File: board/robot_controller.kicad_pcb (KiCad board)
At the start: 2 copper layers, 308 parts, among them J101 CONN_2, J102 CONN_2, J103 CONN_2, J104 JTAG-ARM, J105 CONN_2, J106 USBCONN, J107 CONN_8, J108 CONN_8, J109 USBCONN, J110 CONN_4, J111 UEXT, J112 UEXT, J201 CONN_2, J2301 CONN_STEPPER, J2302 CONN_2, J2401 CONN_STEPPER, J2402 CONN_2, J2501 CONN_STEPPER, J2502 CONN_2, J2601 CONN_STEPPER, J2602 CONN_2, J301 CONN_2, P101 CONN_4, P102 CONN_1, P103 CONN_1, P104 CONN_1, P105 CONN_1, P106 CONN_1, P107 CONN_1, P108 CONN_1, P109 CONN_1, P110 CONN_1, P111 CONN_1, P112 CONN_1, P113 CONN_1, P114 CONN_1, P115 CONN_1, P116 CONN_1, P117 CONN_1, P118 CONN_1, P119 CONN_1, P120 CONN_1, P121 CONN_1, P122 CONN_1, P123 CONN_1, P124 CONN_1, P125 CONN_1, P126 CONN_1, P127 CONN_1, P128 CONN_1, P129 CONN_1, P130 CONN_1, Q101 PNP, Q1501 NJT4031NT1G, Q1601 NJT4031NT1G, Q1701 NJT4031NT1G, Q1801 NJT4031NT1G, Q1901 NJT4031NT1G, Q2001 NJT4031NT1G, Q2101 NJT4031NT1G, Q2201 NJT4031NT1G, Q401 MMBT5962, Q402 MMBT5962, Q501 MMBT5962, Q502 MMBT5962, U101 STM32F405-144, U102 FT232RL, U201 MAX6675, U2301 L6470, U2401 L6470, U2501 L6470, U2601 L6470, U301 MAX6675, U601 LMZ14201, X101 8MHZ

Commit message: Layed out in general where stuff is going to be located.
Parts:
- moved J109 278.8 mm to (43.2, -112.4), turned to 270 degrees
- moved J2302 257.3 mm to (94.6, -38.1), turned to 180 degrees
- moved R2306 254.5 mm to (90.8, -45.1), turned to 270 degrees
- moved R2307 254.2 mm to (93.3, -45.1)
- moved C2304 248.3 mm to (77.8, -48.6)
- moved C2305 248.3 mm to (76.5, -76.2)
- moved C2306 248.3 mm to (76.5, -77.8)
- moved C2308 248.3 mm to (83.8, -77.8)
- moved C2309 248.3 mm to (69.8, -53.7)
- moved C2310 248.3 mm to (82.2, -53.7)
- moved C2311 248.3 mm to (92.4, -78.1)
- moved D2301 248.3 mm to (76.5, -47.9)
- moved R2301 248.3 mm to (71.8, -85.4)
- moved R2303 248.3 mm to (71.8, -81.6)
- moved R2305 248.3 mm to (68.3, -83.5)
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- renumbered P101 to J113
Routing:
- net GND: track 210.8 -> 261.8 mm, vias 77 -> 82
- net +24V: track 373.3 -> 344.6 mm, vias 49 -> 48
- net /LED Data 0/DATA_OUT: track 0.00 -> 16.4 mm
- net /LED Data 1/DATA_OUT: track 0.00 -> 10.3 mm
- net Net-(R127-Pad3): track 0.00 -> 8.26 mm
- net Net-(J2302-Pad2): track 0.00 -> 8.25 mm
- net Net-(Q501-Pad2): track 0.00 -> 7.61 mm
- net Net-(Q401-Pad2): track 0.00 -> 7.61 mm
- net /LED Data 1/DATA_IN: track 0.00 -> 7.13 mm
- net /Stepper 0/ADCIN: track 72.9 -> 79.8 mm
- net Net-(C2315-Pad1): track 36.1 -> 42.9 mm
- net /SUPPLY_SENSE: track 0.00 -> 5.47 mm
- net Net-(Q502-Pad2): track 0.00 -> 4.55 mm
- net +3.3V: track 199.3 -> 194.8 mm
- net Net-(Q402-Pad2): track 0.00 -> 4.28 mm
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
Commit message: Organized MCU components in the layout
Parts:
- moved R115 206.1 mm to (-59.1, 163.5)
- moved R116 170.6 mm to (39.4, 18.7)
- moved D103 140.6 mm to (152.4, 25.1)
- moved D102 137.1 mm to (152.4, 23.2)
- moved D105 122.6 mm to (155.3, 34.0)
- moved R107 117.2 mm to (155.9, 27.0)
- moved D101 115.4 mm to (152.4, 21.3)
- moved R104 113.2 mm to (155.9, 25.1)
- moved R106 112.7 mm to (152.4, 34.0), turned to 180 degrees
- moved R129 112.6 mm to (28.6, 47.9)
- moved X101 109.5 mm to (121.6, 109.2), turned to 270 degrees
- moved R113 103.8 mm to (33.0, 158.8)
- moved R114 101.3 mm to (124.1, 158.8)
- moved R102 100.5 mm to (155.9, 23.2)
- moved D104 96.6 mm to (152.4, 27.0)
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
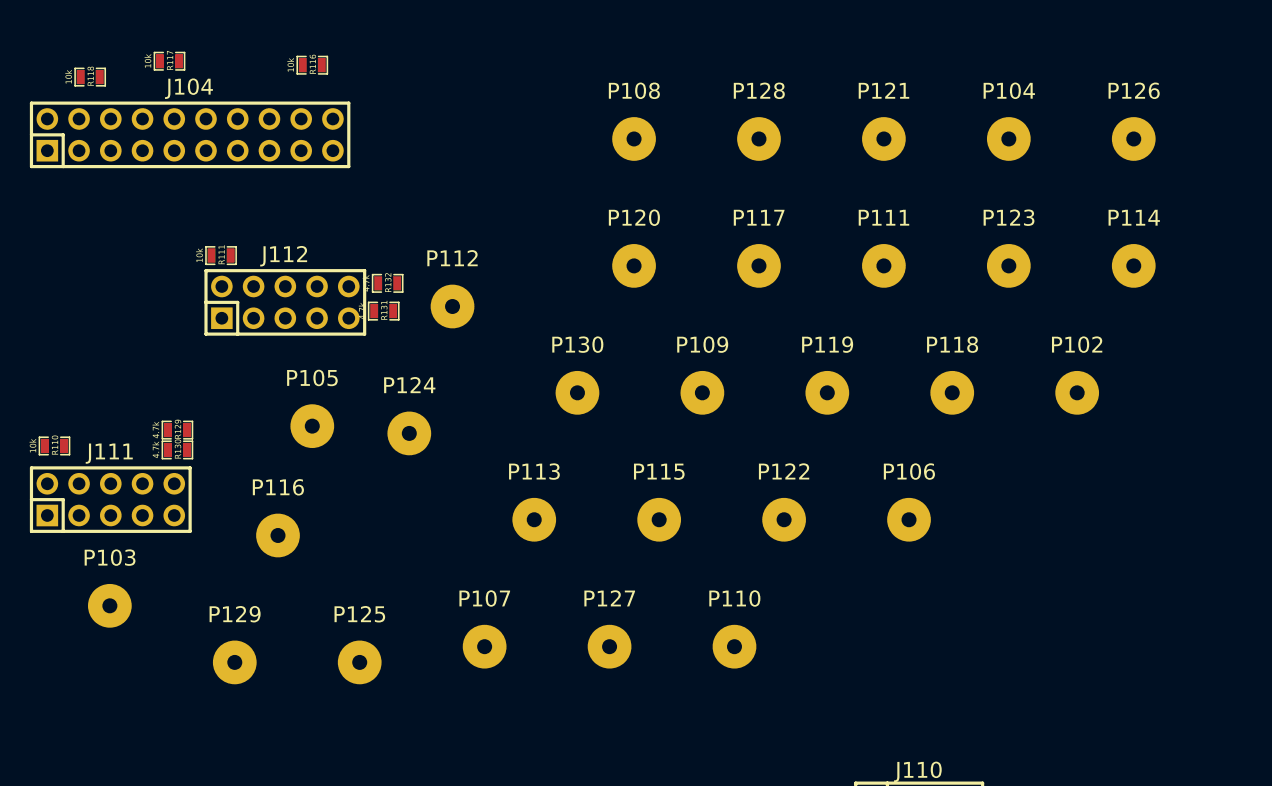
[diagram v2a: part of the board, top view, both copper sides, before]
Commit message: Updated Test Point Footprint on the PCB Layout
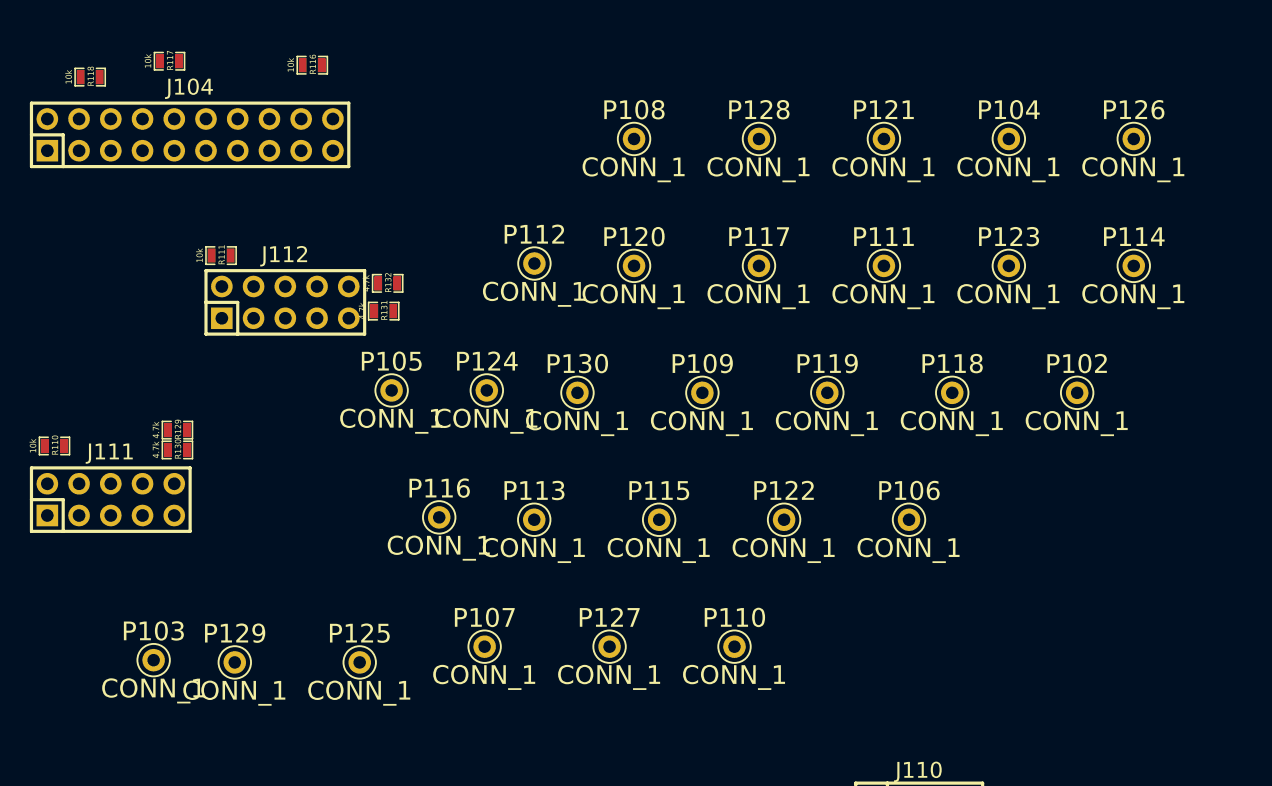
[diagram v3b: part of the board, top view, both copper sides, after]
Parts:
- P102, P103, P104, P105, P106, P107, P108, P109, P110, P111, P112, P113, P114, P115, P116, P117, P118, P119, P120, P121, P122, P123, P124, P125, P126, P127, P128, P129, P130: footprint Wire_Pads:SolderWirePad_single_1-2mmDrill -> components:MINI_TP
- moved P116 13.0 mm to (49.5, 54.9)
- moved P112 7.40 mm to (57.1, 34.6)
- moved P124 7.09 mm to (53.3, 44.8)
- moved P105 6.96 mm to (45.7, 44.8)
- moved P103 5.59 mm to (26.7, 66.4)

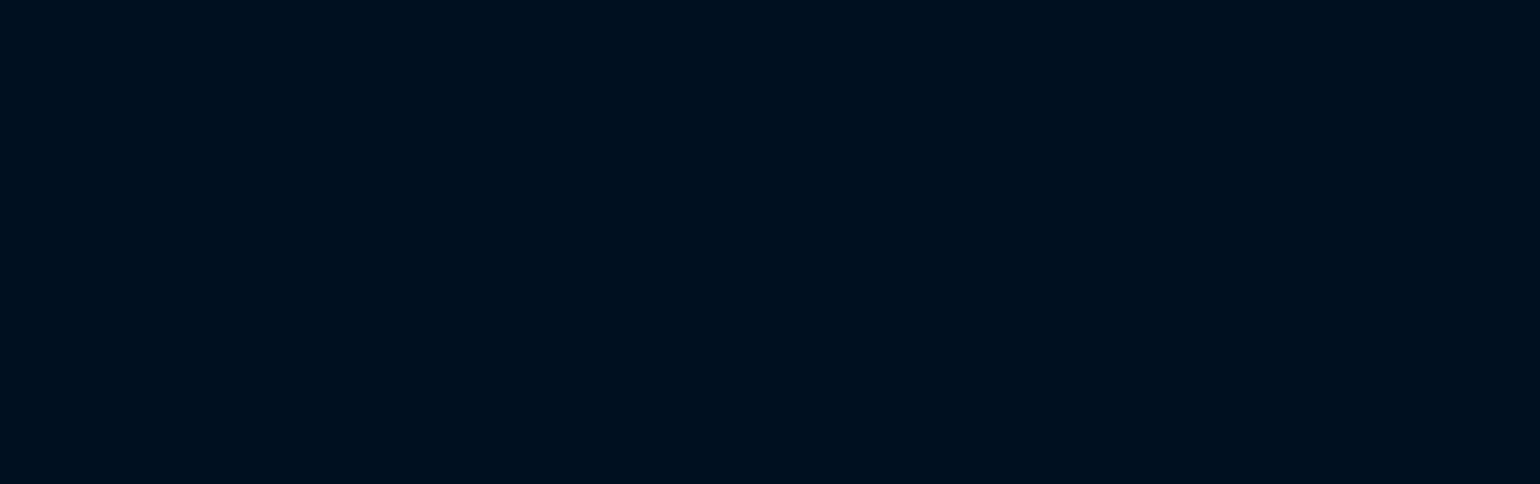
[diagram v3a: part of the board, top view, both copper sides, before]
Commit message: Added pushbuttons to the PCB Layout
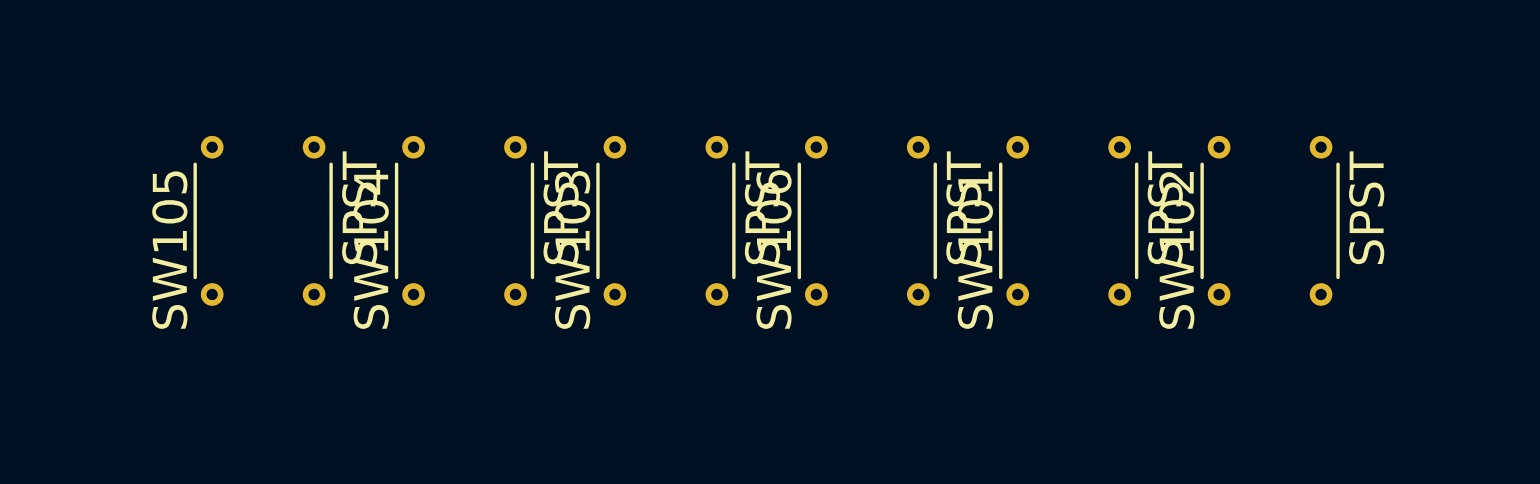
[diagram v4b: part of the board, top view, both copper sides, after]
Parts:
- added SW101: SPST, components:PB, F.Cu at (163.8, 61.3)
- added SW102: SPST, components:PB, F.Cu at (172.7, 61.3)
- added SW103: SPST, components:PB, F.Cu at (146.1, 61.3)
- added SW104: SPST, components:PB, F.Cu at (137.2, 61.3)
- added SW105: SPST, components:PB, F.Cu at (128.3, 61.3)
- added SW106: SPST, components:PB, F.Cu at (154.9, 61.3)
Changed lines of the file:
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@@
 (kicad_pcb (version 3) (host pcbnew "(2014-01-30 BZR 4648)-product")
   (general
-    (links 0)
-    (no_connects 582)
-    (area -73.4568 -152.779801 210.090657 201.0768)
+    (links 781)
+    (no_connects 606)
+    (area 0 0 0 0)
     (thickness 1.6)
     (drawings 0)
     (tracks 1030)
     (zones 0)
-    (modules 308)
+    (modules 314)
     (nets 238)
   )
@@
       (net 68 "/Stepper 0/SCK"))
   )
+  (module components:PB (layer F.Cu)
+    (at 163.83 61.2775)
+    (fp_text reference SW101 (at -4.064 1.27 90) (layer F.SilkS)
+      (effects (font (size 1.5 1.5) (thickness 0.15)))
+    )
+    (fp_text value SPST (at 4.318 -0.508 90) (layer F.SilkS)
+      (effects (font (size 1.5 1.5) (thickness 0.15)))
+    )
+    (fp_line (start 3 -2.5) (end 3 2.5) (layer F.SilkS) (width 0.15))
+    (fp_line (start -3 -2.5) (end -3 2.5) (layer F.SilkS) (width 0.15))
+    (pad 1 thru_hole circle (at -2.25 -3.25) (size 1 1) (drill 0.5) (layers *.Cu *.Mask F.SilkS)
+      (net 2 +3.3V))
+    (pad 1 thru_hole circle (at -2.25 3.25) (size 1 1) (drill 0.5) (layers *.Cu *.Mask F.SilkS)
+      (net 2 +3.3V))
+    (pad 2 thru_hole circle (at 2.25 3.25) (size 1 1) (drill 0.5) (layers *.Cu *.Mask F.SilkS)
+      (net 62 /SW0))
+    (pad 2 thru_hole circle (at 2.25 -3.25) (size 1 1) (drill 0.5) (layers *.Cu *.Mask F.SilkS)
+      (net 62 /SW0))
+  )
+  (module components:PB (layer F.Cu)
+    (at 172.72 61.2775)
+    (fp_text reference SW102 (at -4.064 1.27 90) (layer F.SilkS)
+      (effects (font (size 1.5 1.5) (thickness 0.15)))
+    )
+    (fp_text value SPST (at 4.318 -0.508 90) (layer F.SilkS)
+      (effects (font (size 1.5 1.5) (thickness 0.15)))
+    )
+    (fp_line (start 3 -2.5) (end 3 2.5) (layer F.SilkS) (width 0.15))
+    (fp_line (start -3 -2.5) (end -3 2.5) (layer F.SilkS) (width 0.15))
+    (pad 1 thru_hole circle (at -2.25 -3.25) (size 1 1) (drill 0.5) (layers *.Cu *.Mask F.SilkS)
+      (net 2 +3.3V))
+    (pad 1 thru_hole circle (at -2.25 3.25) (size 1 1) (drill 0.5) (layers *.Cu *.Mask F.SilkS)
+      (net 2 +3.3V))
+    (pad 2 thru_hole circle (at 2.25 3.25) (size 1 1) (drill 0.5) (layers *.Cu *.Mask F.SilkS)
+      (net 63 /SW1))
+    (pad 2 thru_hole circle (at 2.25 -3.25) (size 1 1) (drill 0.5) (layers *.Cu *.Mask F.SilkS)
+      (net 63 /SW1))
+  )
+  (module components:PB (layer F.Cu)
+    (at 146.05 61.2775)
+    (fp_text reference SW103 (at -4.064 1.27 90) (layer F.SilkS)
+      (effects (font (size 1.5 1.5) (thickness 0.15)))
+    )
+    (fp_text value SPST (at 4.318 -0.508 90) (layer F.SilkS)
+      (effects (font (size 1.5 1.5) (thickness 0.15)))
+    )
+    (fp_line (start 3 -2.5) (end 3 2.5) (layer F.SilkS) (width 0.15))
+    (fp_line (start -3 -2.5) (end -3 2.5) (layer F.SilkS) (width 0.15))
+    (pad 1 thru_hole circle (at -2.25 -3.25) (size 1 1) (drill 0.5) (layers *.Cu *.Mask F.SilkS)
+      (net 2 +3.3V))
+    (pad 1 thru_hole circle (at -2.25 3.25) (size 1 1) (drill 0.5) (layers *.Cu *.Mask F.SilkS)
+      (net 2 +3.3V))
+    (pad 2 thru_hole circle (at 2.25 3.25) (size 1 1) (drill 0.5) (layers *.Cu *.Mask F.SilkS)
+      (net 64 /SW2))
+    (pad 2 thru_hole circle (at 2.25 -3.25) (size 1 1) (drill 0.5) (layers *.Cu *.Mask F.SilkS)
+      (net 64 /SW2))
+  )
+  (module components:PB (layer F.Cu)
+    (at 137.16 61.2775)
+    (fp_text reference SW104 (at -4.064 1.27 90) (layer F.SilkS)
+      (effects (font (size 1.5 1.5) (thickness 0.15)))
+    )
+    (fp_text value SPST (at 4.318 -0.508 90) (layer F.SilkS)
+      (effects (font (size 1.5 1.5) (thickness 0.15)))
+    )
+    (fp_line (start 3 -2.5) (end 3 2.5) (layer F.SilkS) (width 0.15))
+    (fp_line (start -3 -2.5) (end -3 2.5) (layer F.SilkS) (width 0.15))
+    (pad 1 thru_hole circle (at -2.25 -3.25) (size 1 1) (drill 0.5) (layers *.Cu *.Mask F.SilkS)
+      (net 2 +3.3V))
+    (pad 1 thru_hole circle (at -2.25 3.25) (size 1 1) (drill 0.5) (layers *.Cu *.Mask F.SilkS)
+      (net 2 +3.3V))
+    (pad 2 thru_hole circle (at 2.25 3.25) (size 1 1) (drill 0.5) (layers *.Cu *.Mask F.SilkS)
+      (net 65 /SW3))
+    (pad 2 thru_hole circle (at 2.25 -3.25) (size 1 1) (drill 0.5) (layers *.Cu *.Mask F.SilkS)
+      (net 65 /SW3))
+  )
+  (module components:PB (layer F.Cu)
+    (at 128.27 61.2775)
+    (fp_text reference SW105 (at -4.064 1.27 90) (layer F.SilkS)
+      (effects (font (size 1.5 1.5) (thickness 0.15)))
+    )
+    (fp_text value SPST (at 4.318 -0.508 90) (layer F.SilkS)
+      (effects (font (size 1.5 1.5) (thickness 0.15)))
+    )
+    (fp_line (start 3 -2.5) (end 3 2.5) (layer F.SilkS) (width 0.15))
+    (fp_line (start -3 -2.5) (end -3 2.5) (layer F.SilkS) (width 0.15))
+    (pad 1 thru_hole circle (at -2.25 -3.25) (size 1 1) (drill 0.5) (layers *.Cu *.Mask F.SilkS)
+      (net 56 /MCU_RESET))
+    (pad 1 thru_hole circle (at -2.25 3.25) (size 1 1) (drill 0.5) (layers *.Cu *.Mask F.SilkS)
+      (net 56 /MCU_RESET))
+    (pad 2 thru_hole circle (at 2.25 3.25) (size 1 1) (drill 0.5) (layers *.Cu *.Mask F.SilkS)
+      (net 119 GND))
+    (pad 2 thru_hole circle (at 2.25 -3.25) (size 1 1) (drill 0.5) (layers *.Cu *.Mask F.SilkS)
+      (net 119 GND))
+  )
+  (module components:PB (layer F.Cu)
+    (at 154.94 61.2775)
+    (fp_text reference SW106 (at -4.064 1.27 90) (layer F.SilkS)
+      (effects (font (size 1.5 1.5) (thickness 0.15)))
+    )
+    (fp_text value SPST (at 4.318 -0.508 90) (layer F.SilkS)
+      (effects (font (size 1.5 1.5) (thickness 0.15)))
+    )
+    (fp_line (start 3 -2.5) (end 3 2.5) (layer F.SilkS) (width 0.15))
+    (fp_line (start -3 -2.5) (end -3 2.5) (layer F.SilkS) (width 0.15))
+    (pad 1 thru_hole circle (at -2.25 -3.25) (size 1 1) (drill 0.5) (layers *.Cu *.Mask F.SilkS)
+      (net 5 /BOOT0))
+    (pad 1 thru_hole circle (at -2.25 3.25) (size 1 1) (drill 0.5) (layers *.Cu *.Mask F.SilkS)
+      (net 5 /BOOT0))
+    (pad 2 thru_hole circle (at 2.25 3.25) (size 1 1) (drill 0.5) (layers *.Cu *.Mask F.SilkS)
+      (net 2 +3.3V))
+    (pad 2 thru_hole circle (at 2.25 -3.25) (size 1 1) (drill 0.5) (layers *.Cu *.Mask F.SilkS)
+      (net 2 +3.3V))
+  )
   (segment (start 62.23 -40.3225) (end 99.06 -40.3225) (width 0.4064) (layer B.Cu) (net 0))
